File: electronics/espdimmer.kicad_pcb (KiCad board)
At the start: 2 copper layers, 86.9 x 18.8 mm, 19 parts, among them J10 LED2, J5 UART, J6 Motion, J7 PWR1, J8 PWR2, J9 LED1, Q1 IRLB3034, Q2 IRLB3034, SW1 Reset, SW2 Flash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

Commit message: Schematics and PCB design updated
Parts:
- PS1: value BUCK -> BUCK_4P; footprint ESPDimmer:XM1584_buck_module -> Buck:XM1584_buck_mod_4p
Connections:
- net Net-(J10-Pad2) renamed /PWR2
- net Net-(J7-Pad2) renamed /PWR1
- J7 pad 1: GND -> GNDD
- J8 pad 1: GND -> GNDD
- PS1 pad 1: GND -> GNDD
- PS1 pad 3: +3V3 -> GND
- Q1 pad 3: GND -> GNDD
- Q2 pad 3: GND -> GNDD
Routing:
- net GND: track 114.9 -> 53.2 mm, vias 1 -> 0
- net GNDD: track 0.00 -> 43.3 mm
- net Net-(Q1-Pad1): track 84.1 -> 94.8 mm
- net +3V3: track 49.5 -> 52.1 mm
- net Net-(Q2-Pad1): track 32.2 -> 31.1 mm
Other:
- net class Default: clearance 0.2 -> 0.25
- net class PWR: clearance 0.2 -> 0.25; trace_width 2 -> 1.8
- net class VCC: clearance 0.2 -> 0.25
- rule trace_clearance: 0.2 -> 0.25

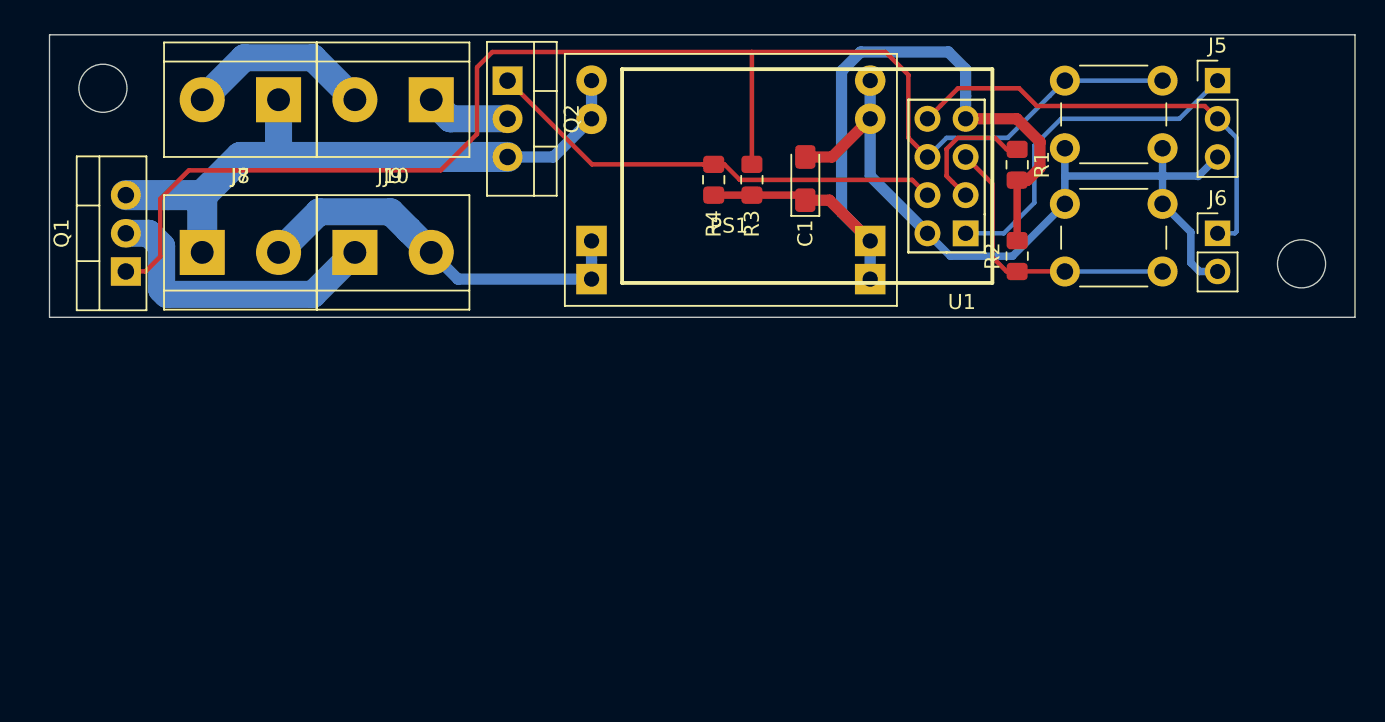
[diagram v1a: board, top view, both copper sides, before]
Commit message: Schematics/PCB updated
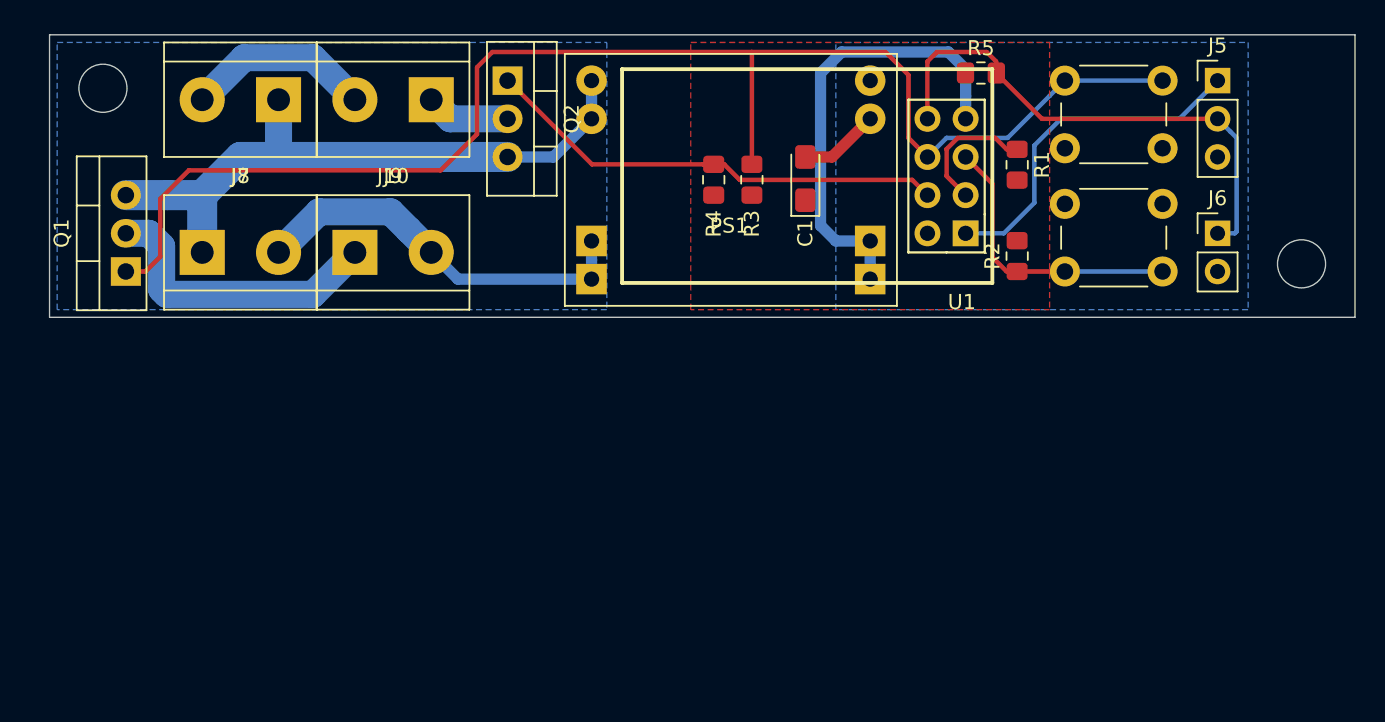
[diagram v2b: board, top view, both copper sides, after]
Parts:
- added R5: 4.7k, Resistor_SMD:R_0805_2012Metric_Pad1.15x1.40mm_HandSolder, F.Cu at (206.8, 121.4)
- R3, R4: value 10k -> 4.7k
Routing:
- net GND: track 53.2 -> 5.37 mm
- net +3V3: track 52.1 -> 30.9 mm
- net Net-(J5-Pad2): track 30.3 -> 35.0 mm
- added copper zone on F.Cu, net +3V3
- added copper zone on B.Cu, net GND
- added copper zone on B.Cu, net GNDD

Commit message: esphome config added
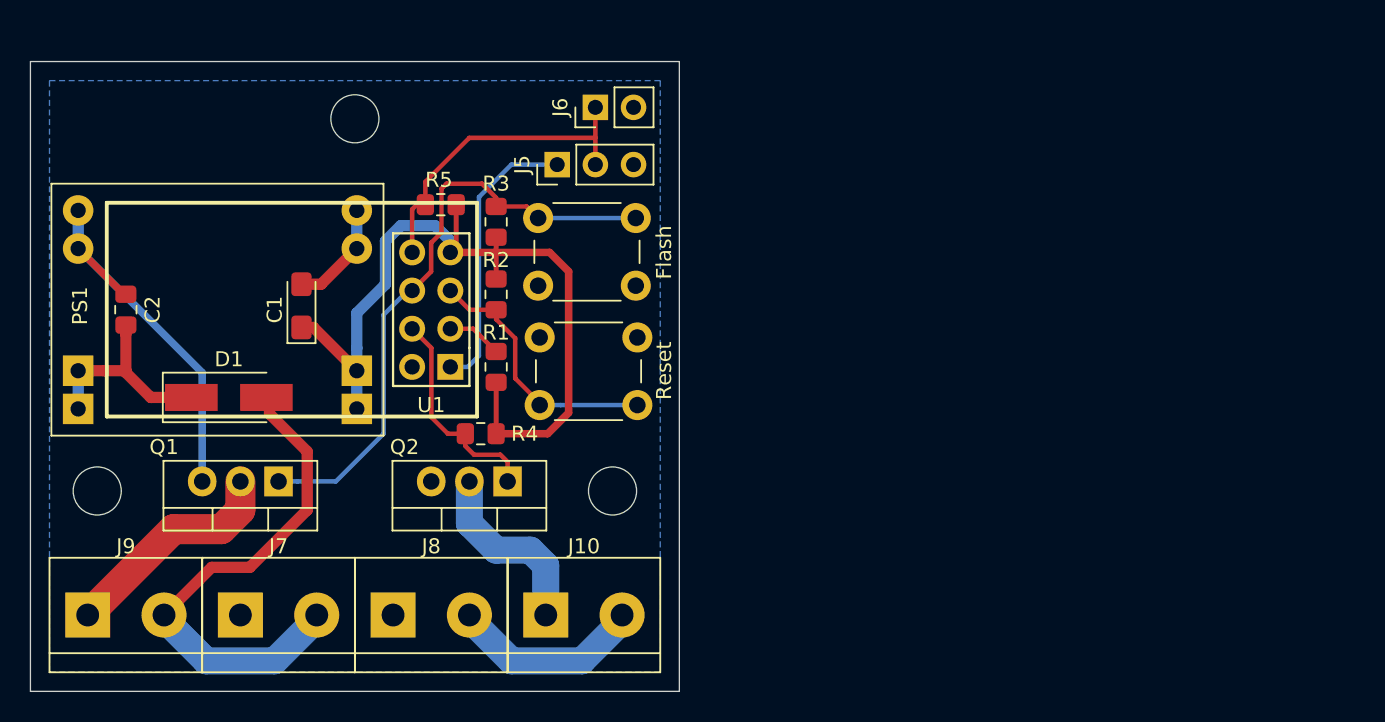
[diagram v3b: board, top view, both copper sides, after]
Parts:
- added C2: 100nF 50V, Capacitor_SMD:C_0805_2012Metric_Pad1.15x1.40mm_HandSolder, F.Cu at (149.9, 137.2)
- added D1: SS14, Diode_SMD:D_SMA_Handsoldering, F.Cu at (156.7, 143.0)
- added REF**: MountingHole_3.2mm_M3, MountingHole:MountingHole_3.2mm_M3, F.Cu at (165.1, 124.5)
- C1: value CP_Small -> 10uF 10V
- moved REF** 48.3 mm to (182.2, 149.2)
- moved J5 44.3 mm to (178.6, 127.5), turned to 90 degrees
- moved J6 42.2 mm to (181.1, 123.7), turned to 90 degrees
- moved R1 37.2 mm to (174.5, 141.0)
- moved R5 37.0 mm to (170.8, 130.2), turned to 180 degrees
- moved SW2 36.2 mm to (177.3, 131.1)
- moved SW1 36.1 mm to (183.9, 143.5)
- moved U1 35.4 mm to (171.4, 141.0)
- moved PS1 35.2 mm to (146.7, 130.6)
- moved J10 35.1 mm to (177.8, 157.5), turned to 0 degrees
- moved J8 35.1 mm to (167.6, 157.5), turned to 0 degrees
- moved R2 34.8 mm to (174.5, 136.1)
- moved C1 34.6 mm to (161.5, 136.9)
- moved J9 30.0 mm to (147.3, 157.5)
- moved REF** 26.8 mm to (148.0, 149.2)
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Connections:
- J7 pad 1: GNDD -> GND
- J8 pad 1: GNDD -> GND
- PS1 pad 1: GNDD -> GND
- PS1 pad 2: /PWR1 -> Net-(C2-Pad1)
- Q1 pad 3: GNDD -> GND
- Q2 pad 3: GNDD -> GND
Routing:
- net Net-(Q1-Pad1): track 94.8 -> 40.7 mm
- net GNDD: track 43.3 -> 0.00 mm
- net GND: track 5.37 -> 33.1 mm
- net +3V3: track 30.9 -> 55.5 mm
- net Net-(Q2-Pad1): track 31.1 -> 14.5 mm
- net Net-(C2-Pad1): track 0.00 -> 13.7 mm
- net Net-(J5-Pad2): track 35.0 -> 21.7 mm
- net /PWR1: track 26.3 -> 33.9 mm
- net Net-(J10-Pad1): track 5.61 -> 12.3 mm
- net Net-(R1-Pad1): track 8.91 -> 3.68 mm
- net Net-(J9-Pad1): track 19.8 -> 15.0 mm
- net Net-(J5-Pad1): track 23.2 -> 18.9 mm
- net Net-(R2-Pad1): track 19.1 -> 17.6 mm
- net /PWR2: track 12.5 -> 13.1 mm
- removed copper zone on F.Cu, net +3V3
- removed copper zone on B.Cu, net GNDD
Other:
- board size 86.9 x 18.8 mm -> 43.2 x 41.9 mm
- rule pad_to_mask_clearance: 0.051 -> 0

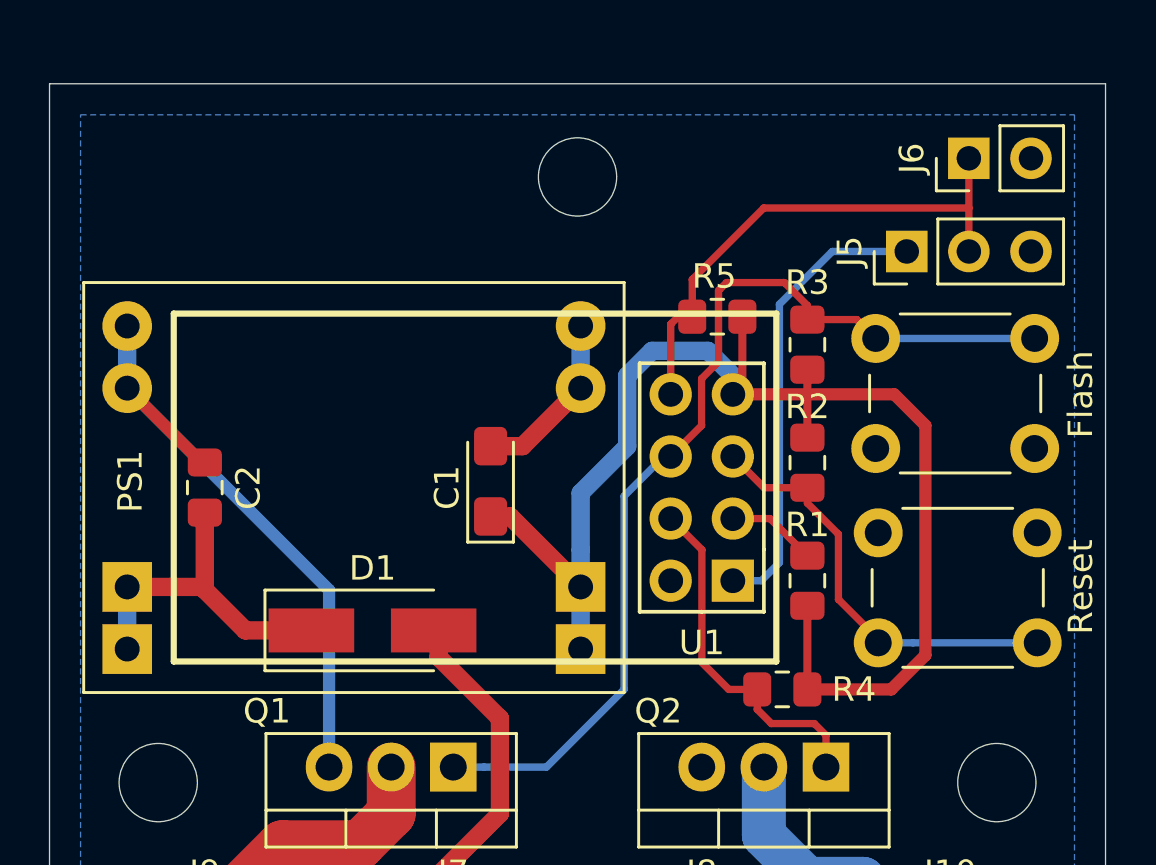
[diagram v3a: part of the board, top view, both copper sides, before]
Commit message: switched to internal esp8266 libs
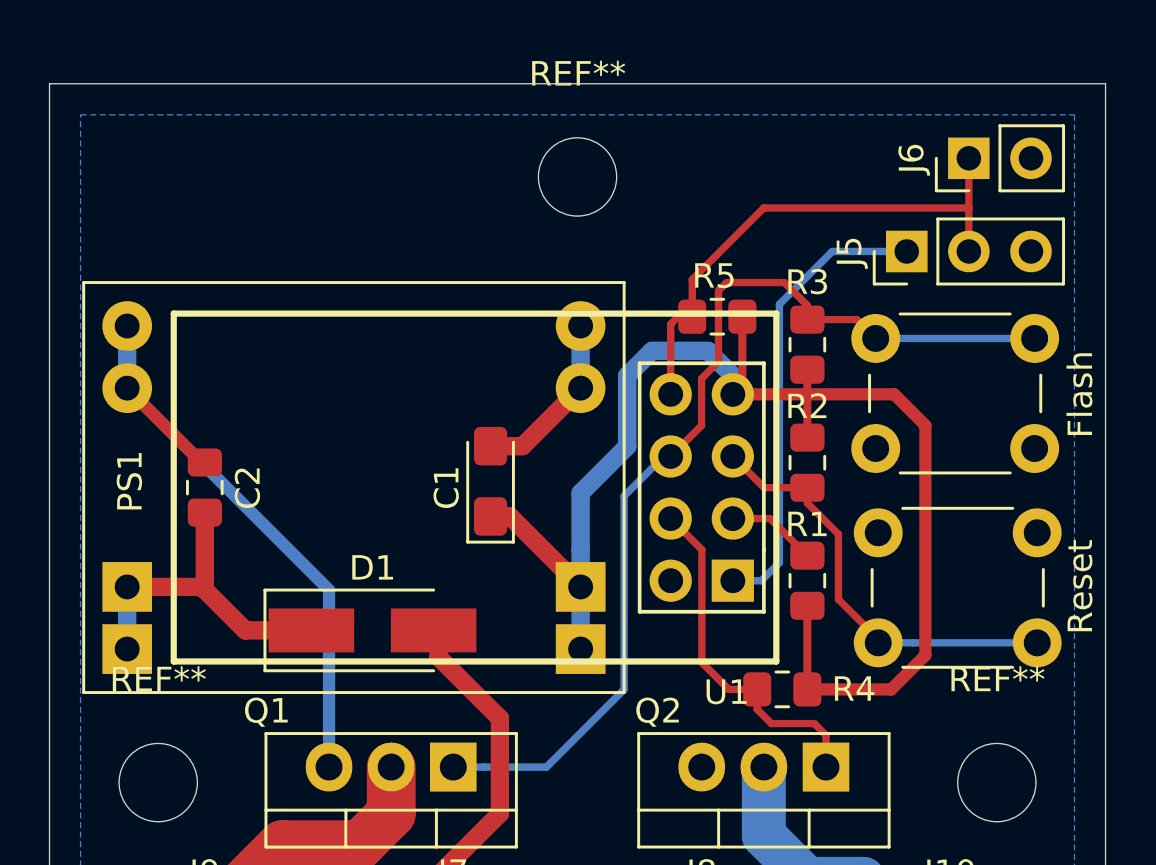
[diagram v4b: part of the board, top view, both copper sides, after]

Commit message: Housing added
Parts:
- added JP1: Jumper_2_Bridged, Jumper:SolderJumper-2_P1.3mm_Open_TrianglePad1.0x1.5mm, B.Cu at (167.6, 153.3)
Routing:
- net GND: track 33.1 -> 9.99 mm
- net /PWR2: track 13.1 -> 19.6 mm
- net /PWR1: track 33.9 -> 39.9 mm
- added copper zone on F.Cu, net GND
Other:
- rule trace_min: 0.3 -> 0.125
